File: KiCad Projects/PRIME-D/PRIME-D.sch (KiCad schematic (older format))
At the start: 33 parts, among them J1 GS2, J10 DropSignal, J2 GS2, J3 Connector_Chamber, J6 BAT1_27V, J7 BAT2_9V, J8 BAT3_27V, J9 CameraTrigger, K1 ORWH-SH-105D1F,000, P1 Power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

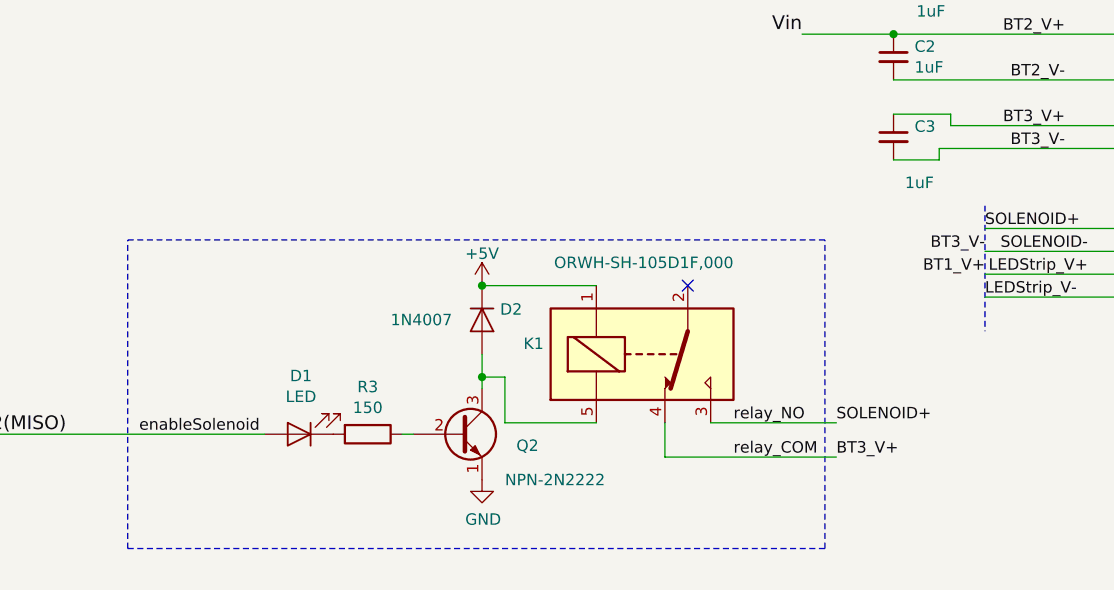
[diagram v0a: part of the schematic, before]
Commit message: Prime D - initial commit R1 - fixed relay pinout
The schematic symbol was incorrect. Easiest solution was to use incorrect schematic symbol and which pins 2 & 3. Should next make both schematic symbol and PCB-layout footprint logically agree with each other.
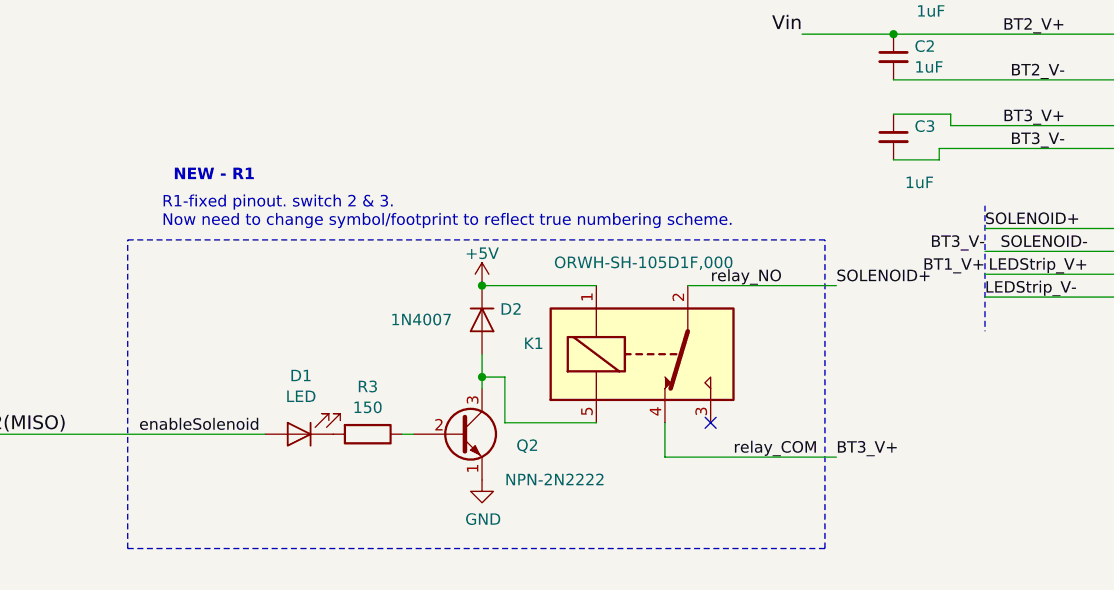
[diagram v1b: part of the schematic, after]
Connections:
- net SOLENOID+: now also K1.2; no longer K1.3
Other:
- note added: "NEW - R1"
- note added: "R1-fixed pinout. switch 2 & 3. \nNow need to change symbol/footprint to reflect true numbering scheme."
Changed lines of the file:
@@
 Sheet 1 1
 Title "PRIME D"
-Date "2019-02-13"
-Rev "0"
+Date "2019-03-06"
+Rev "1"
 Comp "CMR"
 Comment1 "This schematic was created after prototype board was created. "
@@
 Text Label 7550 5900 0    50   ~ 0
 BT3_V+
-NoConn ~ 6900 5150
 Text Label 1050 3150 0    50   ~ 0
 BT1_V-
@@
 	6800 5900 6800 5750
 Wire Wire Line
-	7000 5750 7550 5750
-Wire Wire Line
 	5050 5800 3800 5800
 Text Label 7400 4050 2    60   ~ 0
@@
 Text Notes 5850 2200 0    50   ~ 0
 1. Solenoid+\n2. Solenoid-\n3. X\n4. X \n5. X\n6. X\n7. X\n8. LEDStrip_V-\n9. LEDStrip_V+\n10. X\n11. X\n12. X\n13. X\n14. X\n15. X
-Text Label 7550 5750 0    50   ~ 0
+Text Label 7550 5150 0    50   ~ 0
 SOLENOID+
 Text Label 8200 5000 2    50   ~ 0
@@
 Wire Notes Line
 	4450 4950 7500 4950
-Text Label 7100 5750 0    50   ~ 0
+Text Label 7000 5150 0    50   ~ 0
 relay_NO
 Text Label 7100 5900 0    50   ~ 0
@@
 NoConn ~ 10250 1150
 NoConn ~ 10250 1250
+Wire Wire Line
+	6900 5150 7550 5150
+NoConn ~ 7000 5750
+Text Notes 4600 4900 0    50   ~ 0
+R1-fixed pinout. switch 2 & 3. \nNow need to change symbol/footprint to reflect true numbering scheme.
+Text Notes 4650 4700 0    50   ~ 10
+NEW - R1
 $EndSCHEMATC
